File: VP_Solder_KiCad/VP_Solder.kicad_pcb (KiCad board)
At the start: 2 copper layers, 281 x 94.4 mm, 145 parts, among them J1 Conn_01x04, SW1 SW_Push, SW2 SW_Push, U1 STM32F072CBTx, U2 XC6206PxxxMR, U3 USBLC6-2SC6

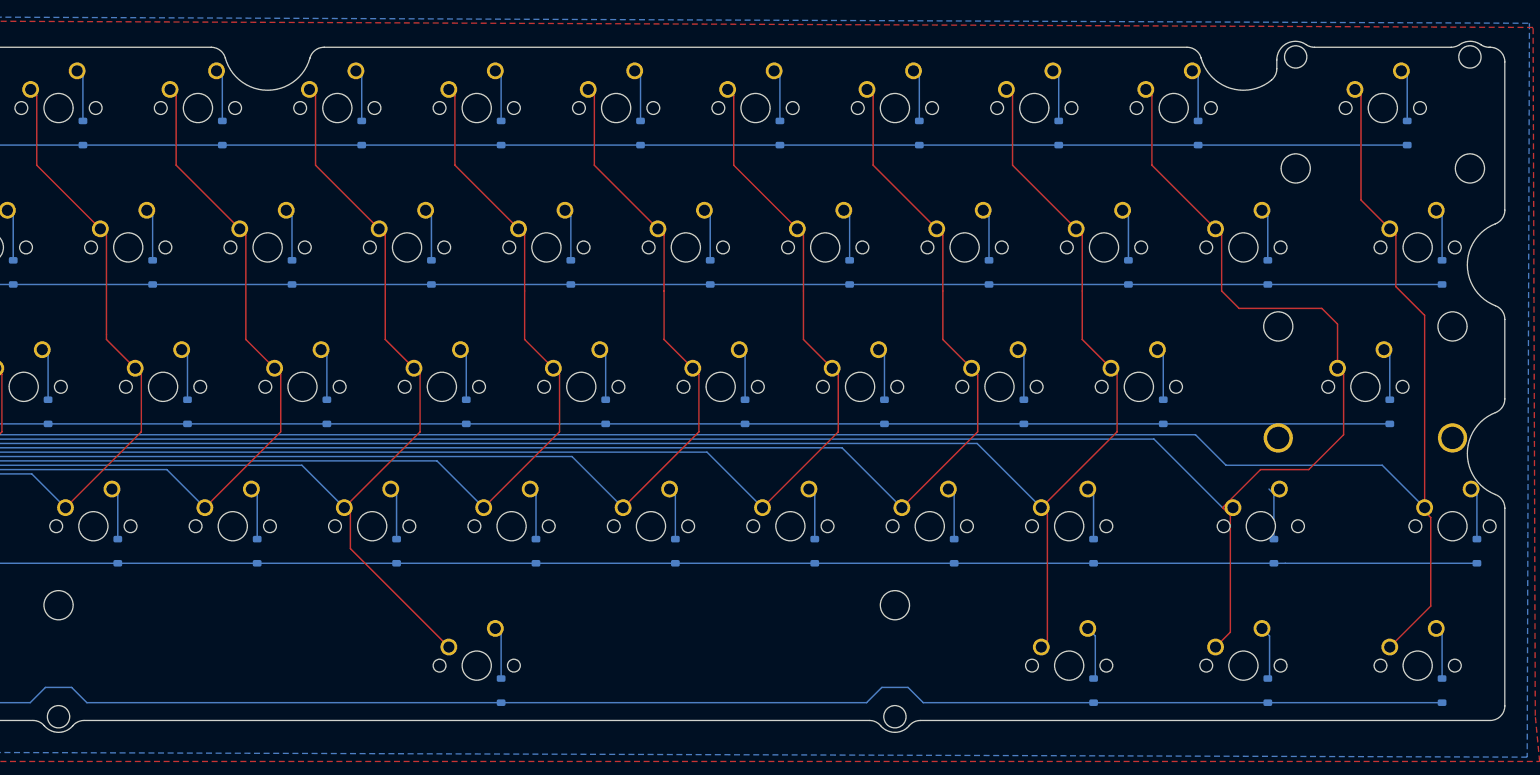
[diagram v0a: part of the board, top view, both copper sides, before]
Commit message: Added split backspace
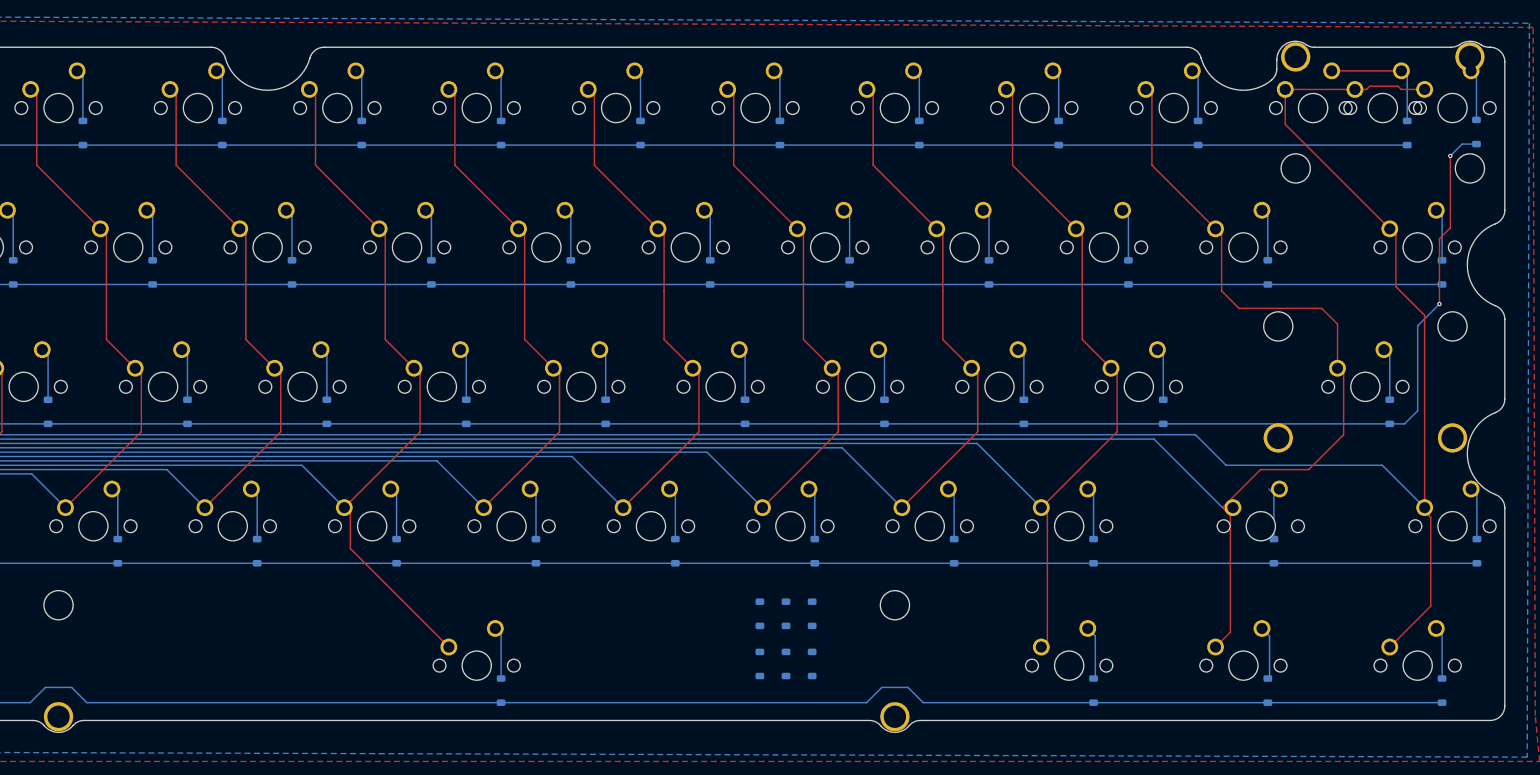
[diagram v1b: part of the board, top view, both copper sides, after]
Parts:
- removed the REF** at (214.3, 154.6)
- removed the REF** at (338.1, 78.4)
- added D42: 1N4148, Diode_SMD:D_SOD-123, B.Cu at (350.9, 81.7)
- added KC_BKSP2: MX_SW_solder, marbastlib-mx:SW_MX_1u, F.Cu at (328.6, 78.4)
- added KC_BSLS2: MX_SW_solder, marbastlib-mx:SW_MX_1u, F.Cu at (347.7, 78.4)
- added REF**: STAB_MX_P_2u, marbastlib-mx:STAB_MX_P_2u, F.Cu at (338.1, 78.4)
- added REF**: D_SOD-123, Diode_SMD:D_SOD-123, B.Cu at (253.0, 154.4)
- added REF**: STAB_MX_P_7u, marbastlib-mx:STAB_MX_P_7u, F.Cu at (214.3, 154.6)
- added REF**: D_SOD-123, Diode_SMD:D_SOD-123, B.Cu at (253.0, 147.5)
- added REF**: D_SOD-123, Diode_SMD:D_SOD-123, B.Cu at (260.2, 147.5)
- added REF**: D_SOD-123, Diode_SMD:D_SOD-123, B.Cu at (256.6, 154.4)
- added REF**: D_SOD-123, Diode_SMD:D_SOD-123, B.Cu at (260.2, 154.4)
- added REF**: D_SOD-123, Diode_SMD:D_SOD-123, B.Cu at (256.6, 147.5)
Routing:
- net /ROW2: track 265.1 -> 310.6 mm, vias 2 -> 4
- net /COL13: track 335.3 -> 359.8 mm
- net Net-(D14-A): track 7.17 -> 16.7 mm
- net Net-(D42-A): track 0.00 -> 7.01 mm
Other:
- board text added: "Extra Diodes"

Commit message: Added testpoints
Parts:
- added TP1: TestPoint, TestPoint:TestPoint_Bridge_Pitch2.0mm_Drill0.7mm, B.Cu at (83.5, 88.5)
- added TP10: TestPoint, TestPoint:TestPoint_Pad_1.5x1.5mm, B.Cu at (226.2, 127.2)
- added TP11: TestPoint, TestPoint:TestPoint_Pad_1.5x1.5mm, B.Cu at (244.7, 126.6)
- added TP12: TestPoint, TestPoint:TestPoint_Pad_1.5x1.5mm, B.Cu at (263.1, 126.0)
- added TP13: TestPoint, TestPoint:TestPoint_Pad_1.5x1.5mm, B.Cu at (281.6, 125.5)
- added TP14: TestPoint, TestPoint:TestPoint_Pad_1.5x1.5mm, B.Cu at (305.7, 124.9)
- added TP15: TestPoint, TestPoint:TestPoint_Pad_1.5x1.5mm, B.Cu at (311.3, 124.3)
- added TP2: TestPoint, TestPoint:TestPoint_Pad_1.5x1.5mm, B.Cu at (84.2, 105.8)
- added TP3: TestPoint, TestPoint:TestPoint_Pad_1.5x1.5mm, B.Cu at (108.3, 110.0)
- added TP4: TestPoint, TestPoint:TestPoint_Pad_1.5x1.5mm, B.Cu at (128.3, 103.4)
- added TP5: TestPoint, TestPoint:TestPoint_Pad_1.5x1.5mm, B.Cu at (146.4, 104.0)
- added TP6: TestPoint, TestPoint:TestPoint_Pad_1.5x1.5mm, B.Cu at (152.4, 129.6)
- added TP7: TestPoint, TestPoint:TestPoint_Pad_1.5x1.5mm, B.Cu at (170.9, 129.0)
- added TP8: TestPoint, TestPoint:TestPoint_Pad_1.5x1.5mm, B.Cu at (189.3, 128.4)
- added TP9: TestPoint, TestPoint:TestPoint_Pad_1.5x1.5mm, B.Cu at (207.8, 127.8)
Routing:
- net /COL12: track 329.8 -> 332.9 mm
- net /COL0: track 109.8 -> 112.7 mm
- net /COL2: track 112.9 -> 115.6 mm, vias 1 -> 2
- net /COL3: track 112.2 -> 114.0 mm, vias 1 -> 2
- net /COL13: track 359.8 -> 361.5 mm
- net /COL11: track 287.1 -> 288.7 mm
- net /COL10: track 248.2 -> 249.9 mm
- net /COL9: track 229.7 -> 231.4 mm
- net /COL8: track 211.2 -> 212.9 mm
- net /COL7: track 195.1 -> 196.8 mm
- net /COL6: track 201.9 -> 203.6 mm
- net /COL5: track 158.8 -> 160.5 mm
- net /COL4: track 144.5 -> 146.1 mm
- net /COL1: track 98.5 -> 100.1 mm
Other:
- board text added: "Velvet Pro Solder PCB v1.0.0 Designed by ShentoBento"

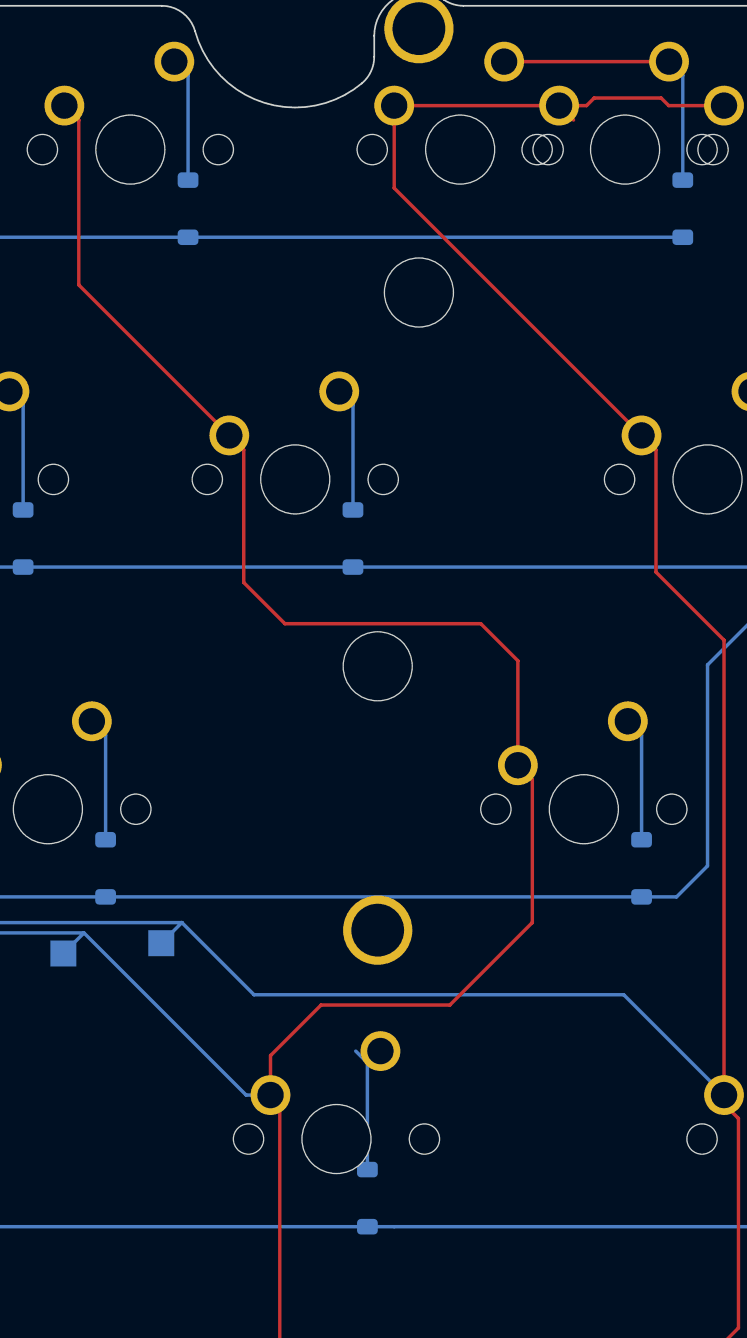
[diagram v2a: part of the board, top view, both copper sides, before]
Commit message: ran drc, fixed some tracing errors
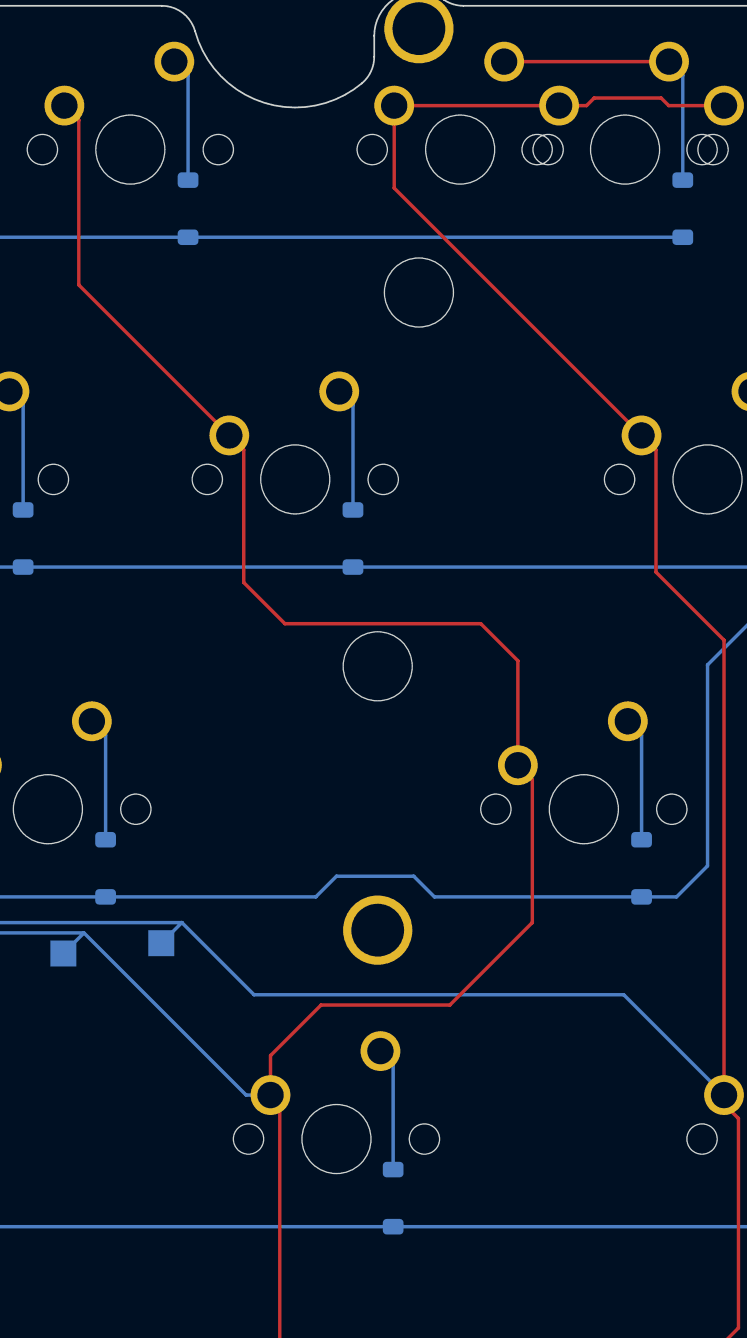
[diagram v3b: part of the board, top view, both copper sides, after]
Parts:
- moved D54 1.49 mm to (324.7, 139.0)
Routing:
- net /COL13: track 361.5 -> 360.3 mm
- net /ROW2: track 310.6 -> 311.6 mm
